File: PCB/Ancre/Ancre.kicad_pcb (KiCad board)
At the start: 2 copper layers, 72.8 x 63 mm, 11 parts, among them IC1 TCAN1051VDRQ1, U1 OKI-78SR-5_1.5-W36-C, U2 DB301V-5.0-2P, U3 DB301V-5.0-2P

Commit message: MaJ PCB ancre pistes
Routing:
- added copper zone on B.Cu, net GNDREF
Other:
- board size 72.8 x 63 mm -> 72.3 x 64 mm
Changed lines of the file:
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@@
 	(gr_rect
 		(start 149.756774 37.5)
-		(end 222.58595 100.5)
+		(end 222.02597 101.5)
 		(stroke
 			(width 0.05)
@@
 		(net "Net-(IC1-RXD)")
 	)
+	(zone
+		(net "GNDREF")
+		(layer "B.Cu")
+		(hatch edge 0.5)
+		(connect_pads
+			(clearance 0.5)
+		)
+		(min_thickness 0.25)
+		(fill yes
+			(thermal_gap 0.5)
+			(thermal_bridge_width 0.5)
+			(island_removal_mode 0)
+		)
+		(polygon
+			(pts
+				(xy 219 100) (xy 155 99.5) (xy 155 95) (xy 150.5 95) (xy 150.5 41.5) (xy 156.5 41.5) (xy 156.5 38.5)
+				(xy 215.5 38.5) (xy 215.5 41.5) (xy 222 41.5) (xy 221.5 97.5) (xy 219 97.5)
+			)
+		)
+	)
 	(embedded_fonts no)

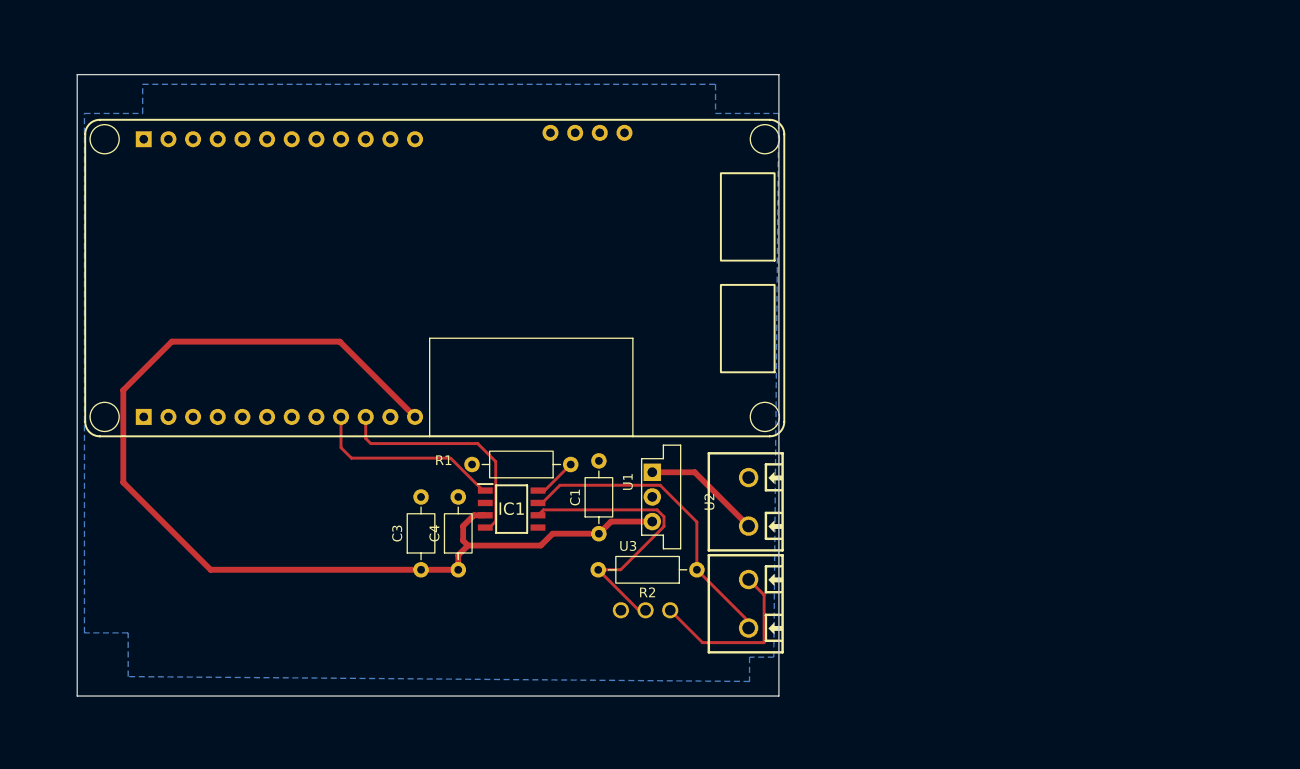
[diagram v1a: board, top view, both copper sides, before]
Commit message: Ajout TCAN bornier bibliotheque
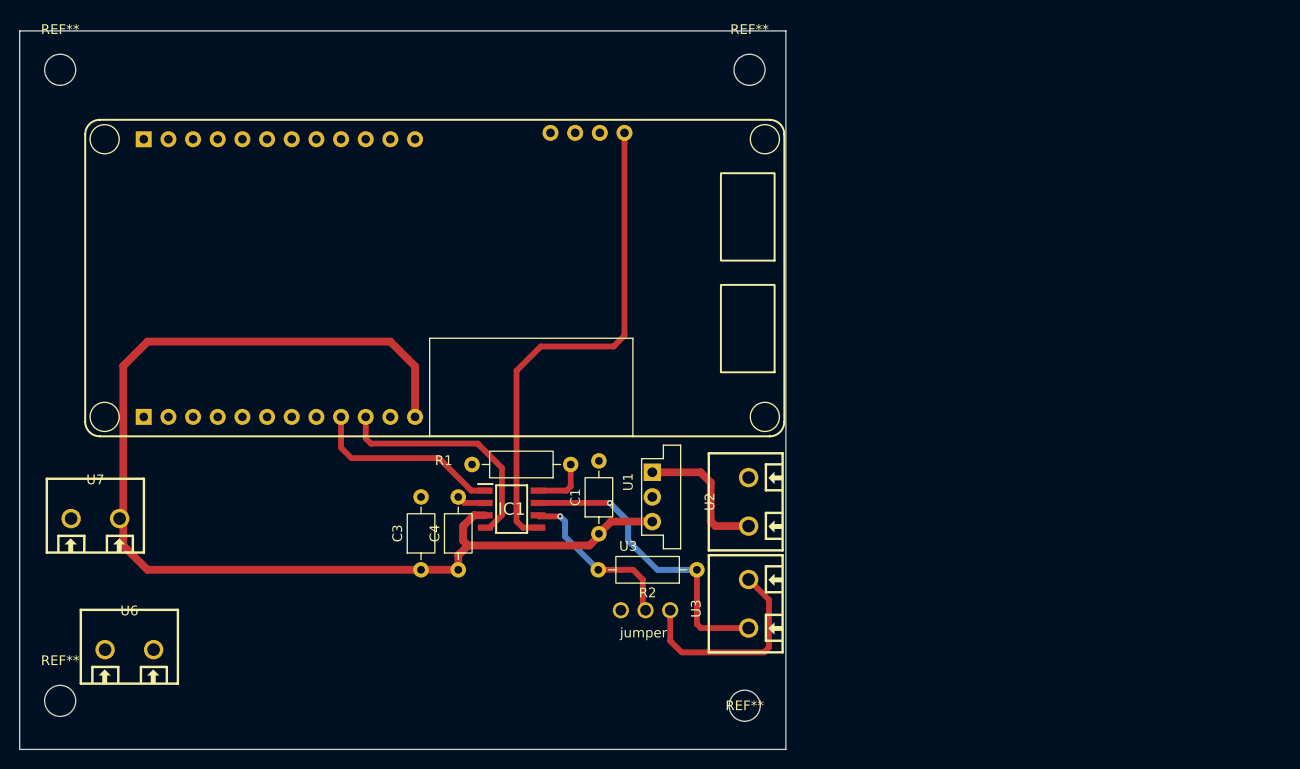
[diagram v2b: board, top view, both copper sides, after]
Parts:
- added REF**: MountingHole_3.2mm_M3, MountingHole:MountingHole_3.2mm_M3, F.Cu at (218.5, 102.5)
- added REF**: MountingHole_3.2mm_M3, MountingHole:MountingHole_3.2mm_M3, F.Cu at (148.0, 37.0)
- added REF**: MountingHole_3.2mm_M3, MountingHole:MountingHole_3.2mm_M3, F.Cu at (148.0, 102.0)
- added REF**: MountingHole_3.2mm_M3, MountingHole:MountingHole_3.2mm_M3, F.Cu at (219.0, 37.0)
- added U6: DB301V-5.0-2P, Bibliotheque_Projet:Bornier a vis, F.Cu at (155.1, 96.7)
- added U7: DB301V-5.0-2P, Bibliotheque_Projet:Bornier a vis, F.Cu at (151.6, 83.2)
- C3, C4: value C -> 100nF
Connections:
- IC1 pad 5: unconnected-(IC1-NC-Pad5) -> Net-(IC1-NC)
- U4 pad 28: unconnected-(U4-3V3-Pad28) -> Net-(IC1-NC)
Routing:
- net Net-(IC1-NC): track 0.00 -> 51.5 mm
- net Net-(IC1-CANL): track 29.7 -> 18.4 mm, vias 0 -> 1
- net +5V: track 110.9 -> 119.4 mm
- net Net-(U5-CAN_line): track 18.2 -> 21.9 mm
- net GNDREF: track 0.00 -> 3.04 mm
- net +12V: track 12.8 -> 15.3 mm
- net Net-(IC1-S): track 4.48 -> 5.81 mm
- net Net-(IC1-CANH): track 31.8 -> 32.6 mm, vias 0 -> 1
- net Net-(IC1-RXD): track 24.1 -> 24.6 mm
- removed copper zone on B.Cu, net GNDREF
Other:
- board size 72.3 x 64 mm -> 78.9 x 74 mm

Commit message: MaJ PCB Ancre
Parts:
- U1: footprint Converter_DCDC:Converter_DCDC_Murata_OKI-78SR_Vertical -> Bibliotheque_Projet:Abaisseur 5v OKI
- moved U6 9.17 mm to (163.5, 93.0), turned to -90 degrees
- moved U7 8.67 mm to (160.0, 81.0), turned to -90 degrees
- moved REF** 6.18 mm to (154.0, 38.5)
- moved REF** 6.08 mm to (154.0, 101.0)
- moved REF** 1.80 mm to (219.5, 101.0)
- moved REF** 1.50 mm to (219.0, 38.5)
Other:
- board size 78.9 x 74 mm -> 72.2 x 69.5 mm

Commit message: finalisation PCB ancre
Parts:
- moved U7 100.7 mm to (259.6, 95.3), turned to 0 degrees
- moved U6 65.8 mm to (229.2, 95.3), turned to 0 degrees
- moved IC1 54.5 mm to (249.0, 82.5), turned to 180 degrees
- moved C3 52.3 mm to (237.2, 83.0), turned to 180 degrees
- moved REF** 51.3 mm to (205.0, 95.5)
- moved REF** 51.2 mm to (205.0, 41.9)
- moved REF** 51.1 mm to (270.0, 41.8)
- moved U4 51.1 mm to (231.4, 63.6)
- moved C1 51.0 mm to (254.2, 89.5), turned to 180 degrees
- moved REF** 50.9 mm to (270.1, 95.4)
- moved U1 49.3 mm to (257.5, 87.1), turned to 90 degrees
- moved C4 49.1 mm to (237.3, 79.8), turned to 180 degrees
- moved R1 38.3 mm to (238.0, 86.1)
- moved U5 35.4 mm to (236.1, 89.8), turned to -90 degrees
- moved U2 33.7 mm to (249.6, 95.3), turned to 0 degrees
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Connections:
- R2 pad 2: Net-(IC1-CANL) -> Net-(U5-Resistance)
- U3 pad 2: Net-(U5-CAN_line) -> Net-(IC1-CANL)
- U5 pad J1: Net-(IC1-CANL) -> Net-(U5-Resistance)
- U5 pad J2: Net-(U5-CAN_line) -> Net-(IC1-CANL)
- U6 pad 1: Net-(IC1-CANH) -> Net-(IC1-CANL)
- U6 pad 2: Net-(U5-CAN_line) -> Net-(IC1-CANH)
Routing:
- net +5V: track 119.4 -> 47.5 mm
- net Net-(U5-CAN_line): track 21.9 -> 0.00 mm
- net Net-(IC1-CANL): track 18.4 -> 39.0 mm
- net Net-(U5-Resistance): track 0.00 -> 18.6 mm
- net Net-(IC1-TXD): track 19.9 -> 35.1 mm, vias 0 -> 2
- net Net-(IC1-S): track 5.81 -> 20.7 mm
- net +12V: track 15.3 -> 26.7 mm
- net GNDREF: track 3.04 -> 13.3 mm
- net Net-(IC1-RXD): track 24.6 -> 33.6 mm, vias 0 -> 1
- net Net-(IC1-CANH): track 32.6 -> 23.8 mm, vias 1 -> 0
- net Net-(IC1-NC): track 51.5 -> 46.9 mm, vias 0 -> 2
- added copper zone on B.Cu, net GNDREF
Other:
- board size 72.2 x 69.5 mm -> 72.2 x 60.7 mm
- board text added: "NAIM.BENRAIES 2026 ESIEE PARIS"
